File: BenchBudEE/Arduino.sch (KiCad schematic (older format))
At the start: 16 parts

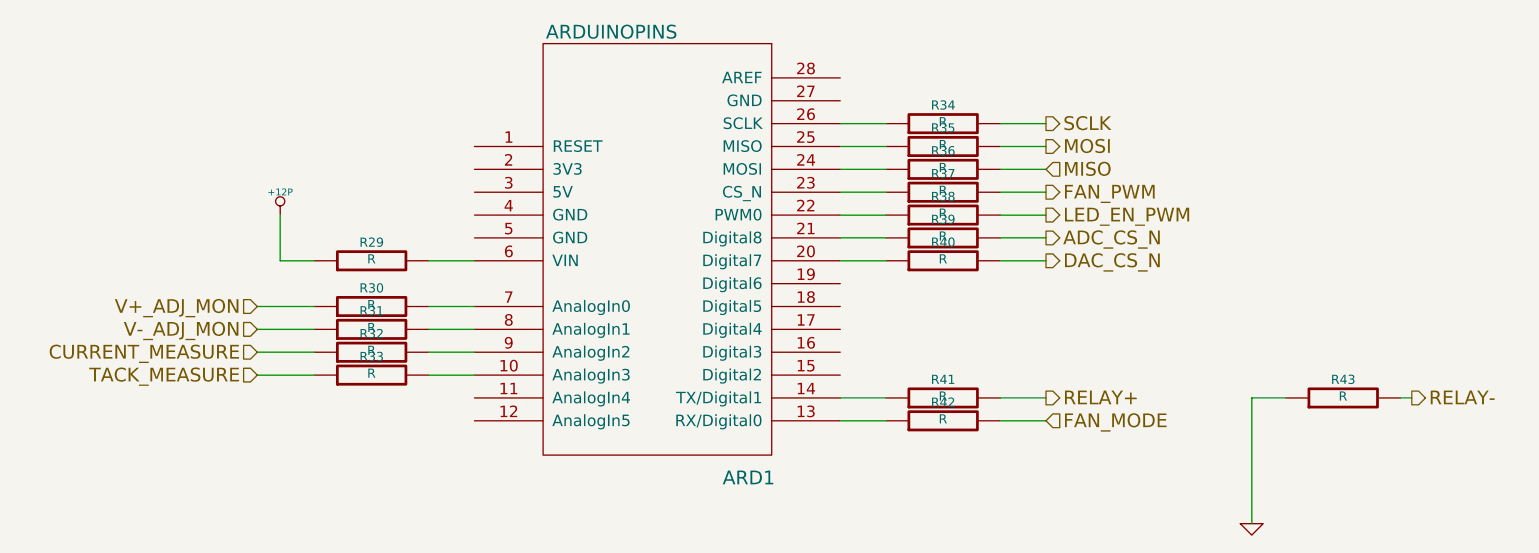
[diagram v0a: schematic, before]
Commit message: Arduino module associated + roughly placed.
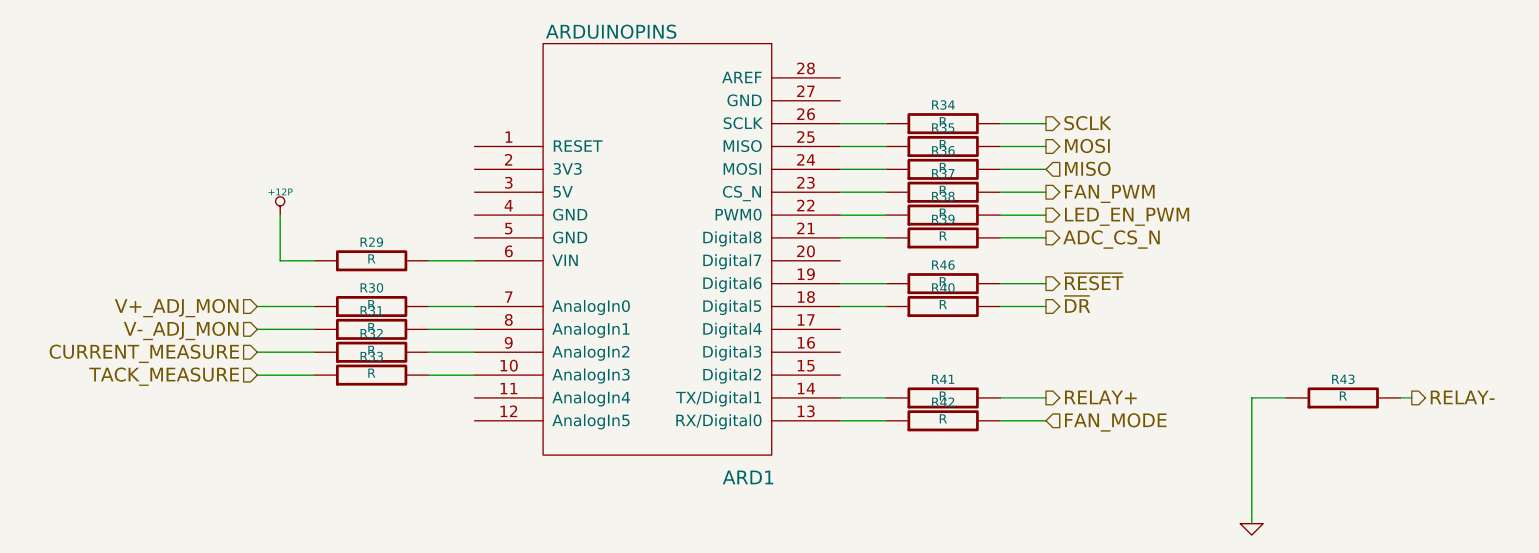
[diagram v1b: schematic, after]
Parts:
- added R46: R, ~, symbol R
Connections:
- net at ARD1.18 (Digital5): now also R40.1
- net at ARD1.19 (Digital6): now also R46.1
- net at ARD1.20 (Digital7): no longer R40.1
- net DAC_CS_N renamed ~DR
- new net ~RESET: R46.2
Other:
- moved on the sheet: R40
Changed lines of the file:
@@
 Sheet 9 9
 Title ""
-Date "20 feb 2014"
+Date "23 feb 2014"
 Rev ""
 Comp ""
@@
 Text HLabel 7700 1800 2    60   Output ~ 0
 SCLK
-Text HLabel 7700 2400 2    60   Output ~ 0
-DAC_CS_N
+Text HLabel 7700 2600 2    60   Output ~ 0
+~DR
 Text HLabel 7700 3000 2    60   Output ~ 0
 RELAY+
@@
 	7000 3000 6800 3000
 $Comp
-L GND #PWR052
+L GND #PWR059
 U 1 1 52F67CCE
 P 8600 3550
-F 0 "#PWR052" H 8600 3550 30  0001 C CNN
+F 0 "#PWR059" H 8600 3550 30  0001 C CNN
 F 1 "GND" H 8600 3480 30  0001 C CNN
 F 2 "" H 8600 3550 60  0000 C CNN
@@
 L R R40
 U 1 1 52F82098
-P 7250 2400
-F 0 "R40" V 7330 2400 40  0000 C CNN
-F 1 "R" V 7257 2401 40  0000 C CNN
-F 2 "~" V 7180 2400 30  0000 C CNN
-F 3 "~" H 7250 2400 30  0000 C CNN
-	1    7250 2400
-	0    -1   -1   0
-$EndComp
-Wire Wire Line
-	7500 2400 7700 2400
-Wire Wire Line
-	7000 2400 6800 2400
+P 7250 2600
+F 0 "R40" V 7330 2600 40  0000 C CNN
+F 1 "R" V 7257 2601 40  0000 C CNN
+F 2 "~" V 7180 2600 30  0000 C CNN
+F 3 "~" H 7250 2600 30  0000 C CNN
+	1    7250 2600
+	0    -1   -1   0
+$EndComp
+Wire Wire Line
+	7500 2600 7700 2600
+Wire Wire Line
+	7000 2600 6800 2600
 Text HLabel 7700 3100 2    60   Input ~ 0
 FAN_MODE
@@
 	5000 2400 5200 2400
 $Comp
-L +12P #PWR053
+L +12P #PWR060
 U 1 1 52F8274D
 P 4350 2200
-F 0 "#PWR053" H 4350 2170 30  0001 C CNN
+F 0 "#PWR060" H 4350 2170 30  0001 C CNN
 F 1 "+12P" H 4350 2300 30  0000 C CNN
 F 2 "" H 4350 2200 60  0000 C CNN
@@
 Wire Wire Line
 	4350 2400 4500 2400
+$Comp
+L R R46
+U 1 1 5307173C
+P 7250 2500
+F 0 "R46" V 7330 2500 40  0000 C CNN
+F 1 "R" V 7257 2501 40  0000 C CNN
+F 2 "~" V 7180 2500 30  0000 C CNN
+F 3 "~" H 7250 2500 30  0000 C CNN
+	1    7250 2500
+	0    -1   -1   0
+$EndComp
+Text HLabel 7700 2500 2    60   Output ~ 0
+~RESET
+Wire Wire Line
+	6800 2500 7000 2500
+Wire Wire Line
+	7500 2500 7700 2500
 $EndSCHEMATC

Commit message: Fan/Current driver associated + roughly placed.
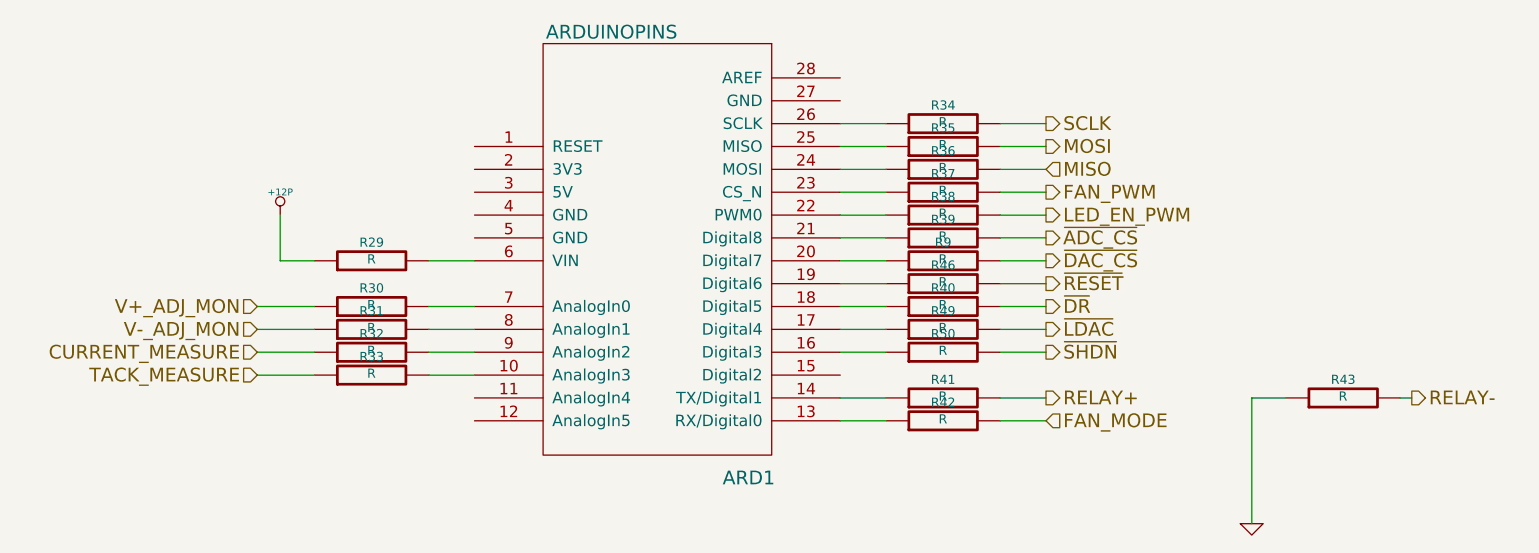
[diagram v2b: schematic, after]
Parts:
- added R49, R50, R9: R, ~, symbol R
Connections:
- net at ARD1.16 (Digital3): now also R50.1
- net at ARD1.17 (Digital4): now also R49.1
- net at ARD1.20 (Digital7): now also R9.1
- net ADC_CS_N renamed ~ADC_CS
- new net ~DAC_CS: R9.2
- new net ~LDAC: R49.2
- new net ~SHDN: R50.2
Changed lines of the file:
@@
 $Descr A4 11693 8268
 encoding utf-8
-Sheet 9 9
+Sheet 8 9
 Title ""
 Date "23 feb 2014"
@@
 	7000 3000 6800 3000
 $Comp
-L GND #PWR059
+L GND #PWR054
 U 1 1 52F67CCE
 P 8600 3550
-F 0 "#PWR059" H 8600 3550 30  0001 C CNN
+F 0 "#PWR054" H 8600 3550 30  0001 C CNN
 F 1 "GND" H 8600 3480 30  0001 C CNN
 F 2 "" H 8600 3550 60  0000 C CNN
@@
 	6800 2300 7000 2300
 Text HLabel 7700 2300 2    60   Output ~ 0
-ADC_CS_N
+~ADC_CS
 Wire Wire Line
 	7500 2300 7700 2300
@@
 	5000 2400 5200 2400
 $Comp
-L +12P #PWR060
+L +12P #PWR055
 U 1 1 52F8274D
 P 4350 2200
-F 0 "#PWR060" H 4350 2170 30  0001 C CNN
+F 0 "#PWR055" H 4350 2170 30  0001 C CNN
 F 1 "+12P" H 4350 2300 30  0000 C CNN
 F 2 "" H 4350 2200 60  0000 C CNN
@@
 Wire Wire Line
 	7500 2500 7700 2500
+$Comp
+L R R49
+U 1 1 530A7461
+P 7250 2700
+F 0 "R49" V 7330 2700 40  0000 C CNN
+F 1 "R" V 7257 2701 40  0000 C CNN
+F 2 "~" V 7180 2700 30  0000 C CNN
+F 3 "~" H 7250 2700 30  0000 C CNN
+	1    7250 2700
+	0    -1   -1   0
+$EndComp
+$Comp
+L R R50
+U 1 1 530A7467
+P 7250 2800
+F 0 "R50" V 7330 2800 40  0000 C CNN
+F 1 "R" V 7257 2801 40  0000 C CNN
+F 2 "~" V 7180 2800 30  0000 C CNN
+F 3 "~" H 7250 2800 30  0000 C CNN
+	1    7250 2800
+	0    -1   -1   0
+$EndComp
+Text HLabel 7700 2700 2    60   Output ~ 0
+~LDAC
+Text HLabel 7700 2800 2    60   Output ~ 0
+~SHDN
+Wire Wire Line
+	6800 2700 7000 2700
+Wire Wire Line
+	6800 2800 7000 2800
+Wire Wire Line
+	7500 2700 7700 2700
+Wire Wire Line
+	7500 2800 7700 2800
+Text HLabel 7700 2400 2    60   Output ~ 0
+~DAC_CS
+$Comp
+L R R9
+U 1 1 530AF318
+P 7250 2400
+F 0 "R9" V 7330 2400 40  0000 C CNN
+F 1 "R" V 7257 2401 40  0000 C CNN
+F 2 "~" V 7180 2400 30  0000 C CNN
+F 3 "~" H 7250 2400 30  0000 C CNN
+	1    7250 2400
+	0    -1   -1   0
+$EndComp
+Wire Wire Line
+	7500 2400 7700 2400
+Wire Wire Line
+	7000 2400 6800 2400
 $EndSCHEMATC
